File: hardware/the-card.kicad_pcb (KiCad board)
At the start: 4 copper layers, 54 x 85.6 mm, 75 parts, among them J1 TYPE-C-31-M-12, J2 FH12-24S-0.5SH(55), J3 S2B-PH-SM4-TB(LF)(SN), Q1 SI2301CDS-T1-GE3, Q2 SI2301CDS-T1-GE3, Q3 SI1308EDL-T1-GE3, SW1 TS-1187A-B-A-B, SW2 TS-1187A-B-A-B, SW3 TS-1187A-B-A-B, SW4 TS-1187A-B-A-B, U1 ESP32-S3-WROOM-1-N16R8, U10 USBLC6-2SC6, U2 ST25DV04KC-IE8S3, U3 LSM6DSOTR, U4 SHT40-BD1B-R2, U5 MAX17048G+T10, U6 TP4056_C382139, U7 DW01A_C18164398, U8 8205A, U9 ME6211C33M5G-N

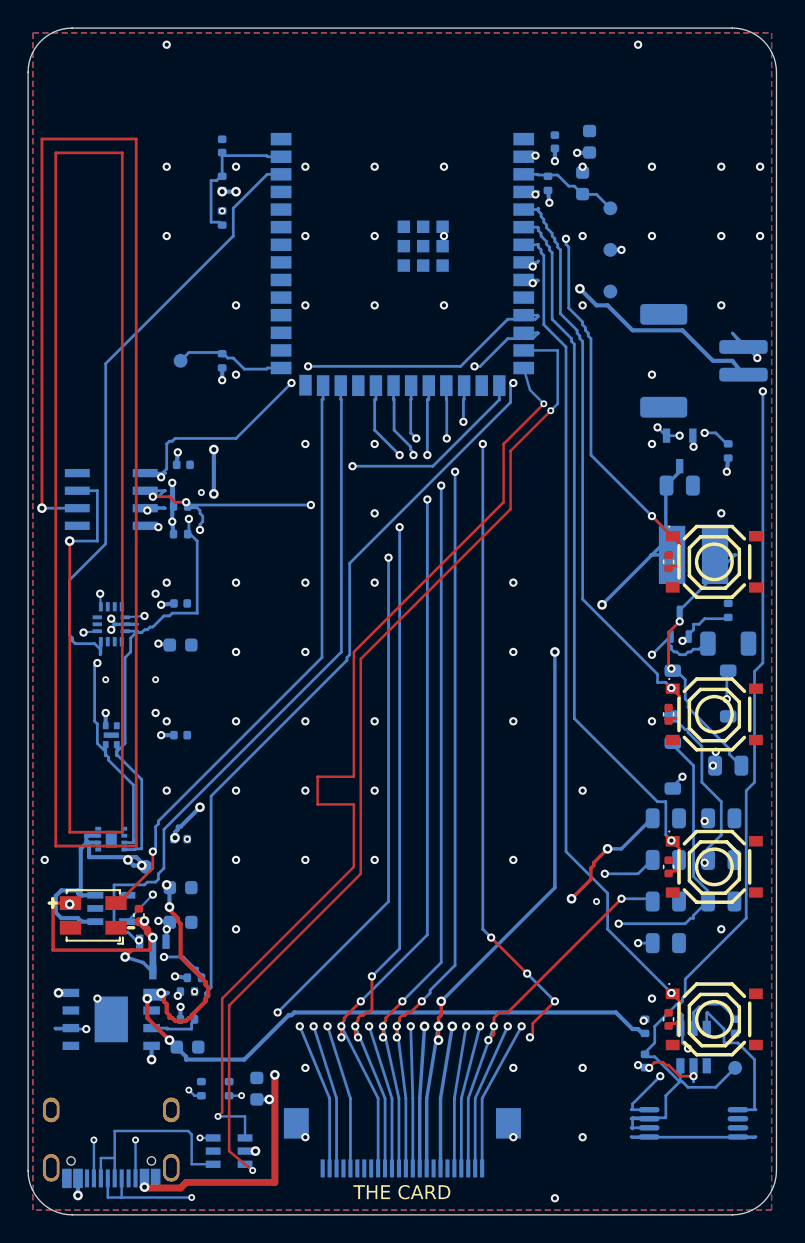
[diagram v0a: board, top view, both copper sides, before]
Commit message: fix(hardware): redesign NFC interface and antenna
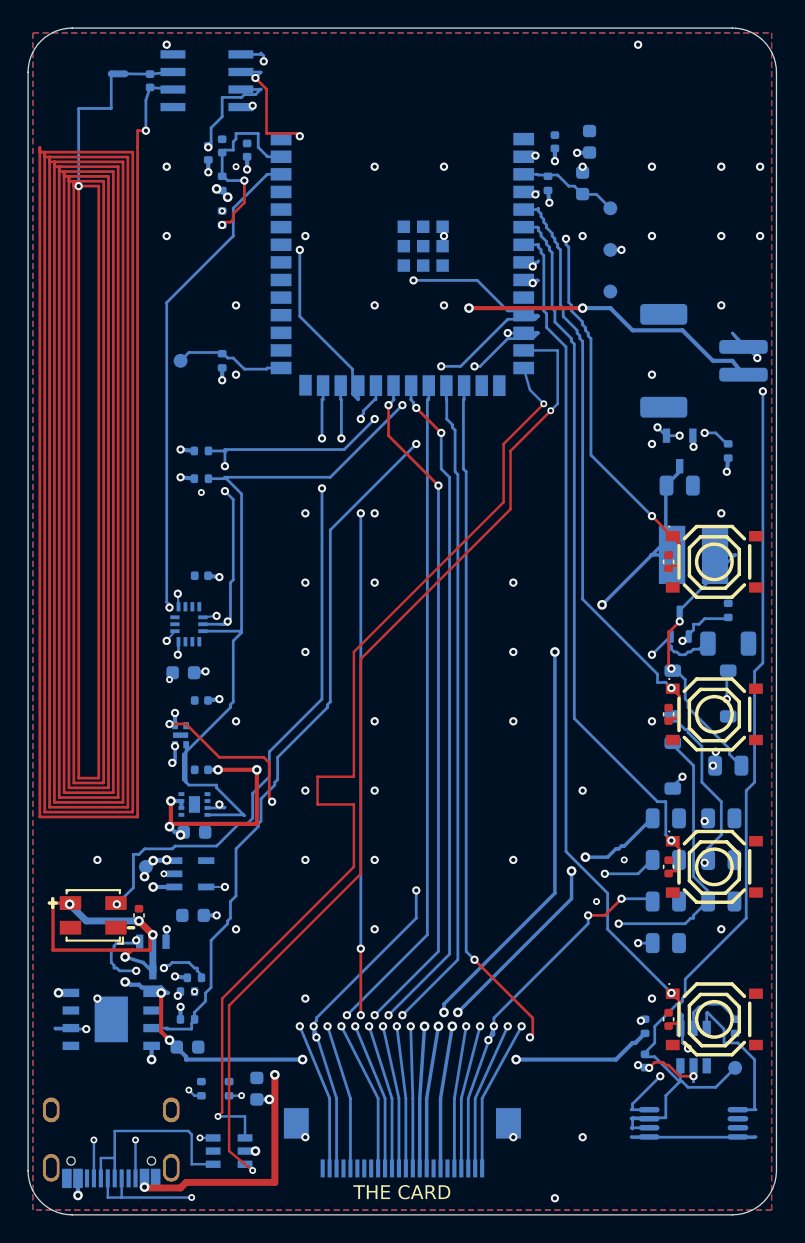
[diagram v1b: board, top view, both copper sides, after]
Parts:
- added C29: DNP 0-22pF C0G/NP0, Capacitor_SMD:C_0402_1005Metric, B.Cu at (28.8, 23.8)
- added L2: PCB NFC antenna, NetTie:NetTie-2_SMD_Pad0.5mm, B.Cu at (26.5, 23.3)
- added R17: 10k, Resistor_SMD:R_0402_1005Metric, B.Cu at (33.0, 29.0)
- moved U2 31.0 mm to (32.9, 23.8)
- moved C11 23.2 mm to (35.8, 28.8), turned to 90 degrees
- moved U5 6.50 mm to (32.0, 76.0)
- moved U9 6.22 mm to (31.7, 81.0)
- moved U3 5.60 mm to (31.6, 63.0)
- moved C10 5.22 mm to (32.5, 73.5), turned to 180 degrees
- moved U4 5.00 mm to (31.0, 71.0)
- moved R13 4.27 mm to (32.5, 50.5)
- moved R14 4.27 mm to (32.5, 52.5)
- moved C8 4.12 mm to (32.0, 78.0)
- moved C14 2.92 mm to (32.5, 68.5), turned to 180 degrees
- moved C12 2.50 mm to (32.5, 59.5), turned to 180 degrees
- moved C13 2.01 mm to (31.2, 66.5), turned to 180 degrees
- moved C9 1.03 mm to (31.9, 84.0), turned to 180 degrees
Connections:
- U1 pad 15: NFC_IRQ -> unconnected-(U1-IO3-Pad15)
- U1 pad 23: unconnected-(U1-IO21-Pad23) -> NFC_IRQ
- U2 pad 2: NFC_ANTENNA -> NFC_AC0
- U2 pad 3: NFC_ANTENNA -> NFC_AC1
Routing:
- net NFC_AC0: track 0.00 -> 911.1 mm, vias 0 -> 2
- net NFC_ANTENNA: track 228.5 -> 0.00 mm, vias 2 -> 0
- net I2C_SDA: track 72.5 -> 100.8 mm
- net I2C_SCL: track 73.0 -> 95.9 mm, vias 8 -> 11
- net EPD_DC: track 70.9 -> 60.6 mm
- net +3V3: track 38.5 -> 47.4 mm, vias 26 -> 27
- net IMU_INT: track 44.2 -> 39.9 mm, vias 0 -> 2
- net LED_DIN: track 43.7 -> 47.2 mm, vias 1 -> 3
- net EPD_RST: track 61.0 -> 57.5 mm
- net NFC_AC1: track 0.00 -> 3.46 mm
- net Net-(U1-IO1): track 11.1 -> 14.4 mm, vias 0 -> 2
- net GND: track 3.60 -> 0.75 mm, vias 74 -> 60
- net PWR_AUX: track 56.6 -> 59.3 mm, vias 2 -> 4
- net NFC_IRQ: track 34.7 -> 32.4 mm
- net EPD_RESE: track 57.9 -> 55.7 mm, vias 2 -> 4
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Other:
- board text added: "REV B - 4L / 0.8 mm"
- board text removed: "REV A - 4L / 0.8 mm"

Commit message: refactor(hardware): unify design versioning
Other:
- board text added: "HW 0.2 - 4L / 0.8 mm"
- board text removed: "REV B - 4L / 0.8 mm"
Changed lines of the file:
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@@
 	(paper "A4")
 	(title_block
-		(rev "B")
+		(rev "0.2.0")
 	)
 	(layers
@@
 		)
 	)
-	(gr_text "REV B - 4L / 0.8 mm"
+	(gr_text "HW 0.2 - 4L / 0.8 mm"
 		(at 47 48.5 0)
 		(layer "B.SilkS")
